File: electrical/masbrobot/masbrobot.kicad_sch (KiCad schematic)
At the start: 24 parts

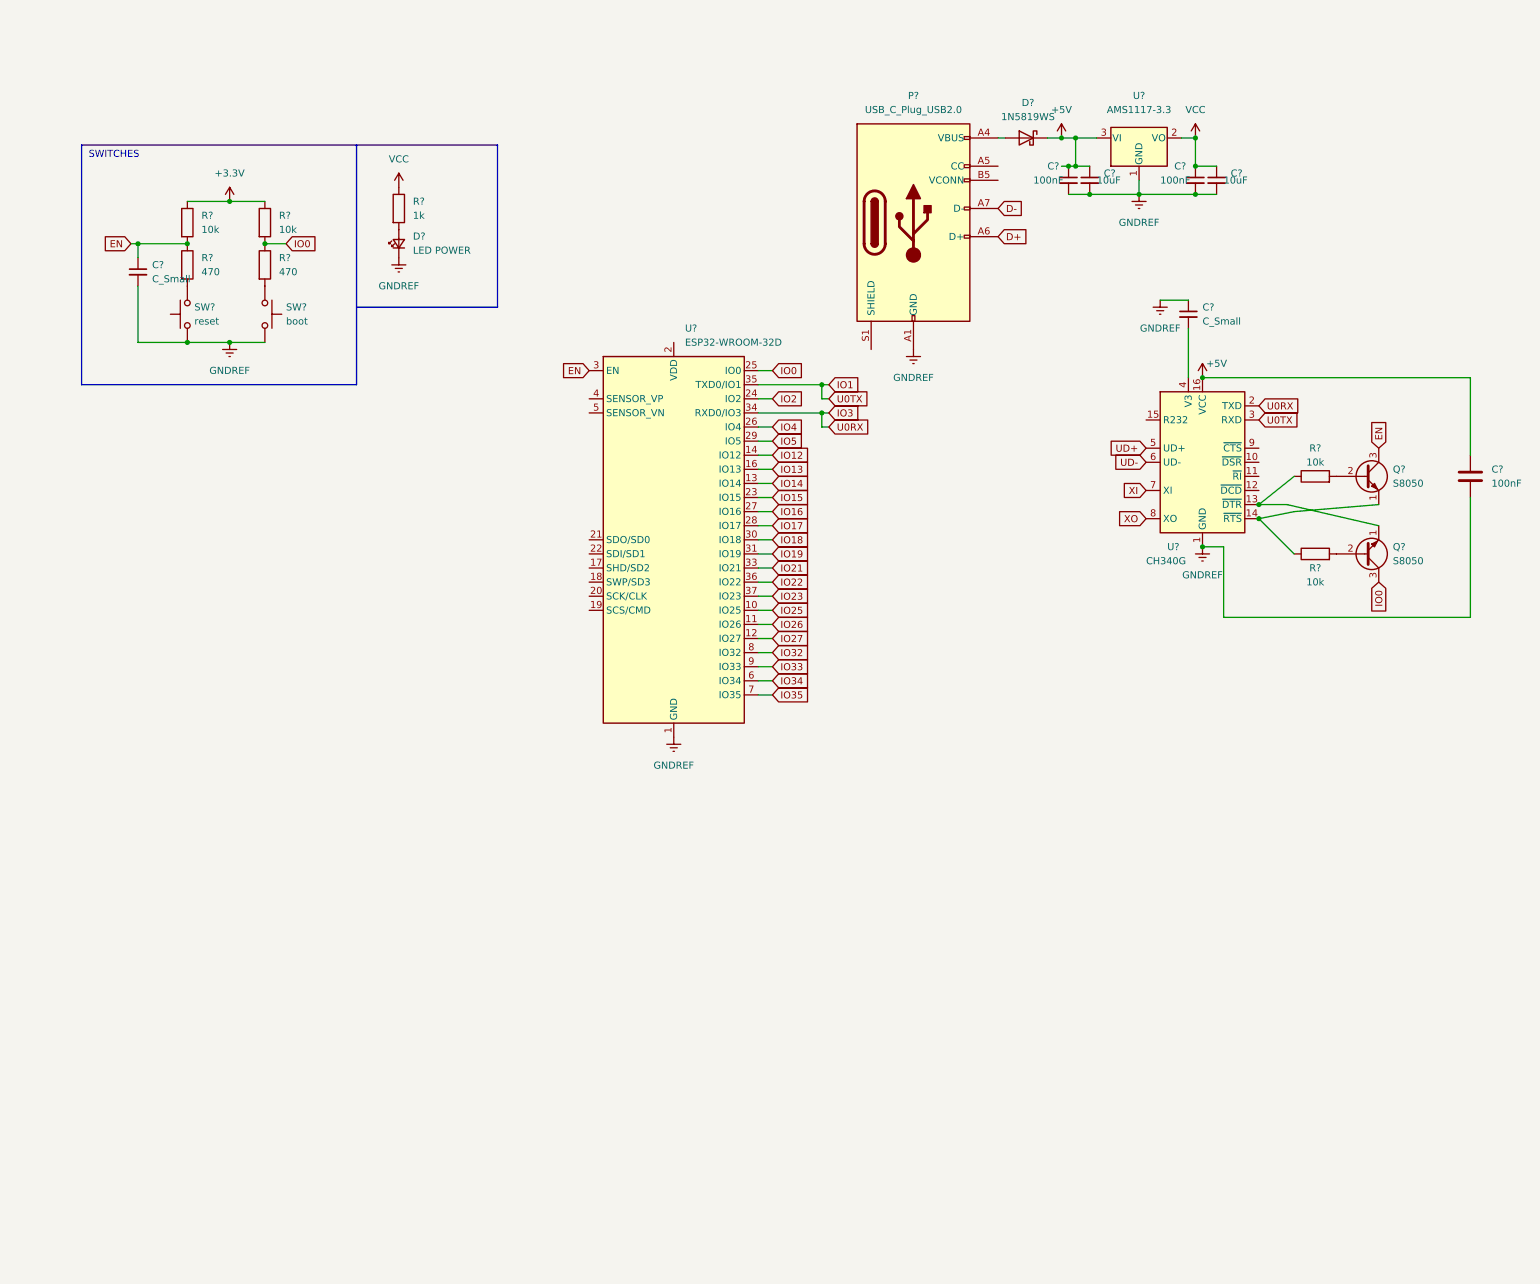
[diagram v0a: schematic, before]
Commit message: adding Gyro schematics, some components, product page link, etc
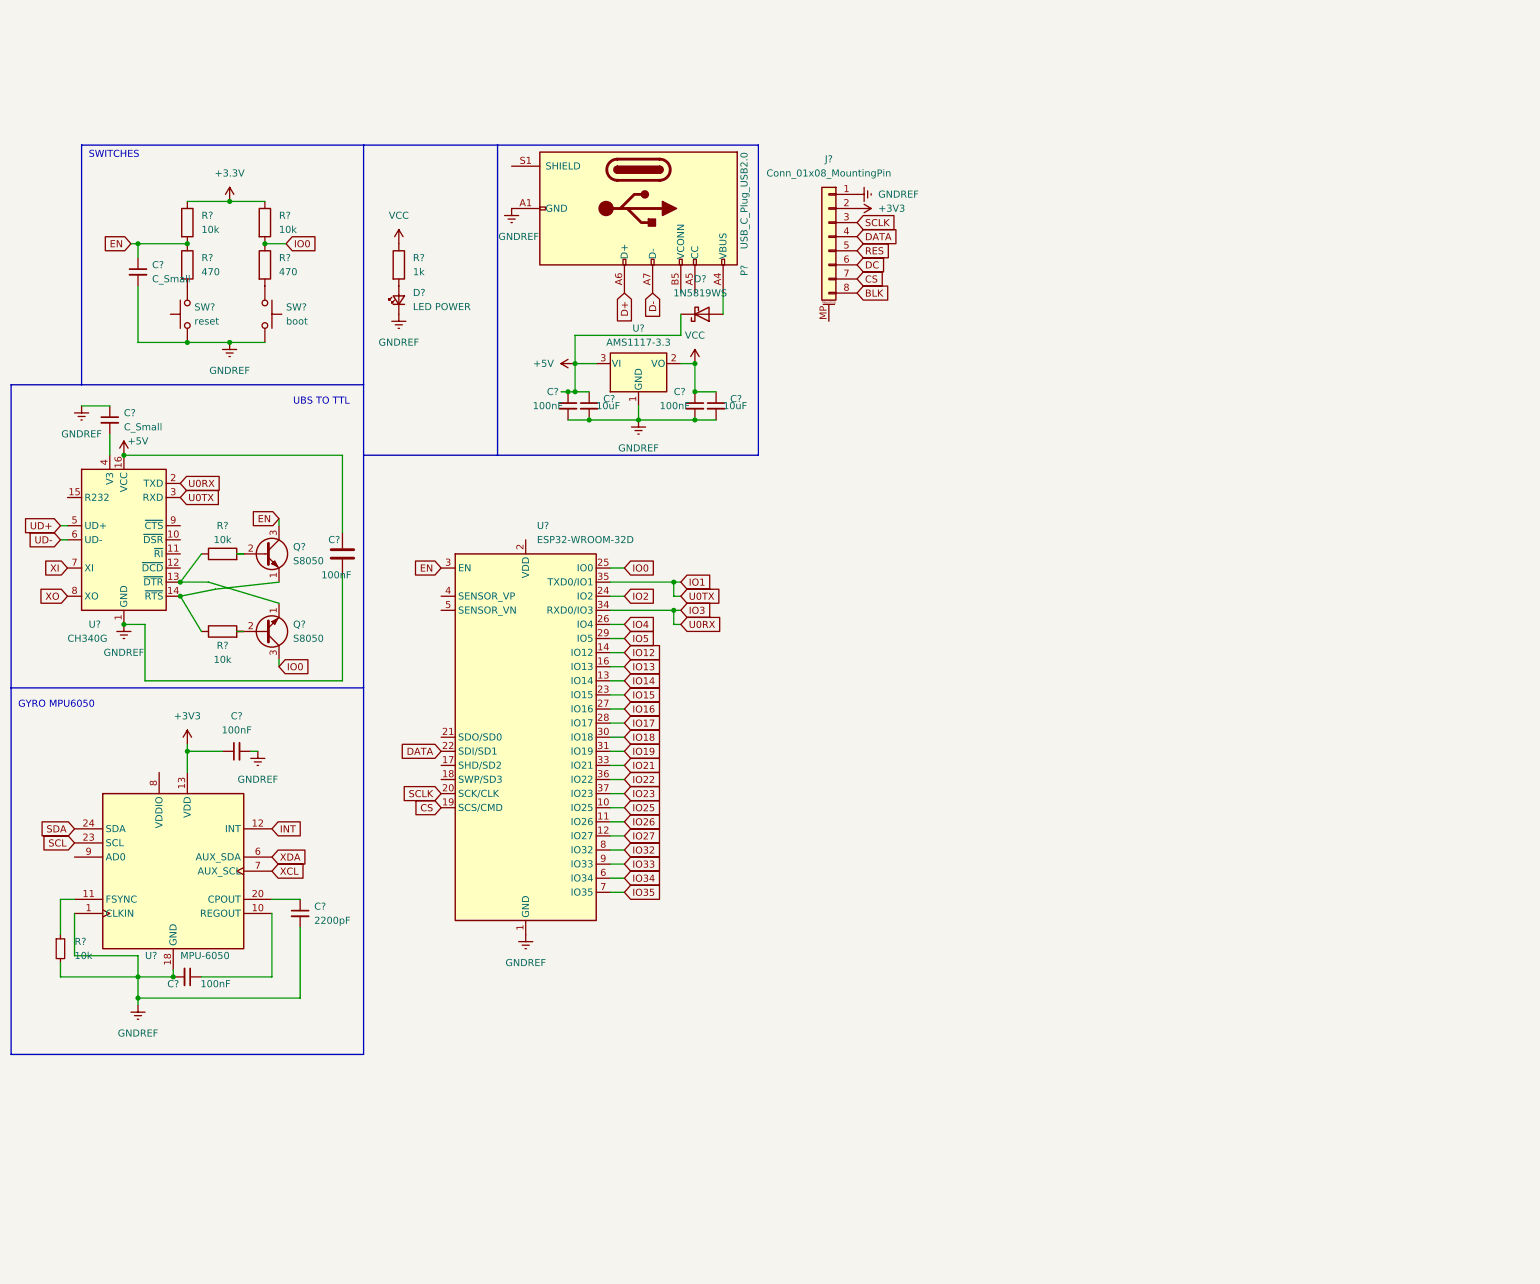
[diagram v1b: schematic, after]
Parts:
- added C? (x2): 100nF, symbol Device:C_Small
- added C?: 2200pF, symbol Device:C_Small
- added J?: Conn_01x08_MountingPin, symbol Connector_Generic_MountingPin:Conn_01x08_MountingPin
- added R?: 10k, symbol Device:R_Small
- added U?: MPU-6050, Sensor_Motion:InvenSense_QFN-24_4x4mm_P0.5mm, symbol Sensor_Motion:MPU-6050
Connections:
- net GNDREF: now also C?.2, C?.2, C?.2, J?.1 (Pin_1), R?.2, U?.1 (CLKIN), U?.18 (GND)
- net CS: now reaches U?.19 (SCS/CMD)
- net CS: now also J?.7 (Pin_7)
- net SCLK: now reaches U?.20 (SCK/CLK)
- net SCLK: now also J?.3 (Pin_3)
- net DATA: now reaches U?.22 (SDI/SD1)
- net DATA: now also J?.4 (Pin_4)
- new net: C?.1, U?.10 (REGOUT)
- new net: C?.1, U?.20 (CPOUT)
- new net: R?.1, U?.11 (FSYNC)
- new net +3V3: C?.1, J?.2 (Pin_2), U?.13 (VDD)
- new net BLK: J?.8 (Pin_8)
- new net DC: J?.6 (Pin_6)
- new net INT: U?.12 (INT)
- new net RES: J?.5 (Pin_5)
- new net SCL: U?.23 (SCL)
- new net SDA: U?.24 (SDA)
- new net XCL: U?.7 (AUX_SCL)
- new net XDA: U?.6 (AUX_SDA)
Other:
- note added: "GYRO MPU6050"
- note added: "UBS TO TTL"
- moved on the sheet: C?, D?, P?, Q?, R?, U?

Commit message: update schematic and PCB board
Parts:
- removed P?: USB_C_Plug_USB2.0, symbol Connector:USB_C_Plug_USB2.0
- added J1: TYPE-C-31-M-12, HRO_TYPE-C-31-M-12, symbol TYPE-C-31-M-12:TYPE-C-31-M-12
- C1, C2: renamed from C?; value C_Small -> 100nF
- C10, C8: renamed from C?; footprint (none) -> Capacitor_SMD:C_0201_0603Metric
- C7, C9: renamed from C?; footprint (none) -> Capacitor_SMD:C_0805_2012Metric
- D1: renamed from D?; footprint (none) -> LED_SMD:LED_0201_0603Metric
- J2: renamed from J?; footprint (none) -> Connector_PinHeader_1.00mm:PinHeader_1x08_P1.00mm_Horizontal
- R1, R3, R6, R7: renamed from R?; footprint (none) -> Resistor_SMD:R_1206_3216Metric
- R8: renamed from R?; footprint (none) -> Resistor_SMD:R_0201_0603Metric
- SW1, SW2: renamed from SW?; footprint (none) -> Button_Switch_SMD:SW_Tactile_SPST_NO_Straight_CK_PTS636Sx25SMTRLFS
- gave numbers to parts that had none: 14
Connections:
- net IO21 is gone; now on net SDA: U3.33 (IO21)
- net IO22 is gone; now on net SCL: U3.36 (IO22)
- net UD+ is gone; now on net D+: U1.5 (UD+)
- net UD- is gone; now on net D-: U1.6 (UD-)
- net +3.3V: now also U3.2 (VDD)
- net D+: now also J1.A6 (DP1)
- net D-: now also J1.A7 (DN1)
- net GNDREF: now also J1.A1_B12 (GND), J1.B1_A12 (GND)
- net at D2.2 (A): now also J1.A4_B9 (VBUS), J1.B4_A9 (VBUS)
- new net: J1.S1 (SHIELD), J1.S2 (SHIELD), J1.S3 (SHIELD), J1.S4 (SHIELD)
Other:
- moved on the sheet: U3

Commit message: update electrial FIX.
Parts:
- added C11, C12, C7: 100nF, Capacitor_SMD:C_0805_2012Metric, symbol Device:C_Small
- added C14, C9: 10uF, Capacitor_SMD:C_0201_0603Metric, symbol Device:C_Small
- added D10, D3, D4, D5, D6, D7, D8, D9: 1N4007, Diode_SMD:D_0201_0603Metric, symbol Diode:1N4007
- added J2: connector battery 2S Li-Po, Connector_JST:JST_XH_S3B-XH-A-1_1x03_P2.50mm_Horizontal, symbol Connector:Conn_01x03_Socket
- added J3: Micro_SD_Card, Connector_Card:microSD_HC_Hirose_DM3BT-DSF-PEJS, symbol Connector:Micro_SD_Card
- added J5, J6: Conn_01x06, Connector_JST:JST_GH_BM06B-GHS-TBT_1x06-1MP_P1.25mm_Vertical, symbol Connector_Generic:Conn_01x06
- added J7: OLED_128x64_I2C, Connector_JST:JST_GH_BM04B-GHS-TBT_1x04-1MP_P1.25mm_Vertical, symbol Connector:Conn_01x04_Socket
- added U4: L298P, L298P:SOIC127P1420X360-20N, symbol Driver_Motor:L298P
- added U5: AMS1117-5.0, Package_TO_SOT_SMD:SOT-223-3_TabPin2, symbol Regulator_Linear:AMS1117-5.0
- C1, C2, C3, C4, C5, C6: footprint (none) -> Capacitor_SMD:C_0805_2012Metric
- D2: renamed from D1; footprint LED_SMD:LED_0201_0603Metric -> LED_SMD:LED_1206_3216Metric
- J1: footprint HRO_TYPE-C-31-M-12 -> TYPE-C-31-M-12:HRO_TYPE-C-31-M-12
- J4: renamed from J2; value Conn_01x08_MountingPin -> IO; footprint Connector_PinHeader_1.00mm:PinHeader_1x08_P1.00mm_Horizontal -> Connector_PinHeader_1.27mm:PinHeader_1x08_P1.27mm_Horizontal
- R1: renamed from R2; footprint (none) -> Resistor_SMD:R_0805_2012Metric
- R4, R5: footprint (none) -> Resistor_SMD:R_0805_2012Metric
- R8: value 1k -> R_LED; footprint Resistor_SMD:R_0201_0603Metric -> Resistor_SMD:R_0402_1005Metric
- renumbered C8 to C10, C9 to C13, C10 to C15, C7 to C8, D2 to D1, R1 to R2, U4 to U6
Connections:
- net +3V3 is gone; now on net +3.3V: C4.1, J4.2 (Pin_2), U2.13 (VDD)
- net BLK is gone; now on net IO35: J4.8 (Pin_8)
- net DC is gone; now on net IO33: J4.6 (Pin_6)
- net IO5 is gone; now on net CS: U3.29 (IO5)
- net RES is gone; now on net IO33: J4.5 (Pin_5)
- net VCC is gone; now on net +3.3V: C13.1, C15.1, R8.1, U6.2 (VO)
- net +3.3V: now also J5.2 (Pin_2), J6.2 (Pin_2)
- net +5V: now also C11.2, C12.1, C14.1, D3.1 (K), D4.1 (K), D5.1 (K), D6.1 (K), J3.4 (VDD), J7.1 (Pin_1), U4.14 (EnB), U4.6 (Vs), U4.8 (EnA), U5.2 (VO)
- net CS: now also J3.2 (DAT3/CD); no longer J4.7 (Pin_7)
- net DATA: no longer J4.4 (Pin_4)
- net GNDREF: now also C11.1, C12.2, C14.2, C7.2, C9.2, D10.2 (A), D7.2 (A), D8.2 (A), D9.2 (A), J2.1 (Pin_1), J3.6 (VSS), J5.5 (Pin_5), J6.5 (Pin_5), J7.4 (Pin_4), U4.1 (GND), U4.10 (GND), U4.11 (GND), U4.19 (SENSE_B), U4.2 (SENSE_A), U4.20 (GND), U5.1 (GND)
- net IO0: no longer U3.25 (IO0)
- net IO27: now also J4.3 (Pin_3)
- net IO32: now also J4.4 (Pin_4)
- net IO34: now also J4.7 (Pin_7)
- net SCL: now also J7.3 (Pin_3)
- net SCLK: no longer J4.3 (Pin_3)
- net SDA: now also J7.2 (Pin_2)
- net IO12 renamed IN4
- net IN4: now also U4.15 (IN4)
- net IO18 renamed SCK
- net SCK: now also J3.5 (CLK)
- net IO19 renamed MISO
- net MISO: now also J3.7 (DAT0)
- net IO2 renamed IN2
- net IN2: now also U4.9 (IN2)
- net IO23 renamed MOSI
- net MOSI: now also J3.3 (CMD)
- net IO4 renamed IN3
- net IN3: now also U4.13 (IN3)
- net XI: no longer names the net of U1.7 (XI)
- net XO: no longer names the net of U1.8 (XO)
- new net +7.5V: C7.1, C9.1, J2.3 (Pin_3), U4.12 (Vss), U5.3 (VI)
- new net EN1A: J6.3 (Pin_3)
- new net EN1B: J6.4 (Pin_4)
- new net EN2A: J5.3 (Pin_3)
- new net EN2B: J5.4 (Pin_4)
- new net IN1: U3.25 (IO0), U4.7 (IN1)
- new net M1A: D3.2 (A), D7.1 (K), J6.1 (Pin_1), U4.4 (OUT1)
- new net M1B: D4.2 (A), D8.1 (K), J6.6 (Pin_6), U4.5 (OUT2)
- new net M2A: D5.2 (A), D9.1 (K), J5.1 (Pin_1), U4.16 (OUT3)
- new net M2B: D10.1 (K), D6.2 (A), J5.6 (Pin_6), U4.17 (OUT4)
- no-connect marks 0 -> 26
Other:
- note added: "Connectors"
- note added: "LED INDICATOR"
- note added: "Micro SD"
- note added: "Microcontroller"
- note added: "Motor Driver L298P"
- note added: "POWER"
- note added: "reserved ext I/O"
- company: (none) -> TRKB/FTMM/Universitas Airlangga
- title: (none) -> Schematic Masbrobot, PCB 1
- moved on the sheet: C1, C10, C13, C15, C2, C3, C4, C5, C6, C8, D1, D2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

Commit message: update smentara
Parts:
- J2: footprint Connector_JST:JST_XH_S3B-XH-A-1_1x03_P2.50mm_Horizontal -> Connector_JST:JST_XH_B3B-XH-A_1x03_P2.50mm_Vertical
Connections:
- net IO13 is gone; now on net EN1A: U3.16 (IO13)
- net IO14 is gone; now on net EN1B: U3.13 (IO14)
- net IO15 is gone; now on net EN2A: U3.23 (IO15)
- net IO16 is gone; now on net EN2B: U3.27 (IO16)
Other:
- title: Schematic Masbrobot, PCB 1 -> Schematic Masbrobot
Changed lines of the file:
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@@
   (paper "User" 279.4 279.4)
   (title_block
-    (title "Schematic Masbrobot, PCB 1")
+    (title "Schematic Masbrobot")
     (date "2023-05-31")
     (rev "0.1")
@@
   )
   (wire (pts (xy 104.14 87.63) (xy 104.14 101.6))
-    (stroke (width 0) (type default))
+    (stroke (width 0) (type default) (color 255 0 7 1))
   )
   (polyline (pts (xy 182.88 167.64) (xy 182.88 77.47))
@@
   )
   (wire (pts (xy 64.77 87.63) (xy 104.14 87.63))
-    (stroke (width 0) (type default))
+    (stroke (width 0) (type default) (color 255 0 2 1))
   )
   (wire (pts (xy 149.86 138.43) (xy 152.4 138.43))
@@
     (effects (font (size 1.27 1.27)) (justify left bottom))
   )
-  (global_label "IO15" (shape input) (at 152.4 115.57 0) (fields_autoplaced)
-    (effects (font (size 1.27 1.27)) (justify left))
-    (property "Intersheetrefs" "${INTERSHEET_REFS}" (at 159.1674 115.4906 0)
+  (global_label "EN2A" (shape input) (at 152.4 115.57 0) (fields_autoplaced)
+    (effects (font (size 1.27 1.27)) (justify left))
+    (property "Intersheetrefs" "${INTERSHEET_REFS}" (at 160.0834 115.57 0)
       (effects (font (size 1.27 1.27)) (justify left) hide)
     )
@@
     )
   )
-  (global_label "IO13" (shape input) (at 152.4 110.49 0) (fields_autoplaced)
-    (effects (font (size 1.27 1.27)) (justify left))
-    (property "Intersheetrefs" "${INTERSHEET_REFS}" (at 159.1674 110.4106 0)
-      (effects (font (size 1.27 1.27)) (justify left) hide)
-    )
-  )
-  (global_label "IO16" (shape input) (at 152.4 118.11 0) (fields_autoplaced)
-    (effects (font (size 1.27 1.27)) (justify left))
-    (property "Intersheetrefs" "${INTERSHEET_REFS}" (at 159.1674 118.0306 0)
+  (global_label "EN1A" (shape input) (at 152.4 110.49 0) (fields_autoplaced)
+    (effects (font (size 1.27 1.27)) (justify left))
+    (property "Intersheetrefs" "${INTERSHEET_REFS}" (at 160.0834 110.49 0)
+      (effects (font (size 1.27 1.27)) (justify left) hide)
+    )
+  )
+  (global_label "EN2B" (shape input) (at 152.4 118.11 0) (fields_autoplaced)
+    (effects (font (size 1.27 1.27)) (justify left))
+    (property "Intersheetrefs" "${INTERSHEET_REFS}" (at 160.2648 118.11 0)
       (effects (font (size 1.27 1.27)) (justify left) hide)
     )
@@
     )
   )
-  (global_label "IO14" (shape input) (at 152.4 113.03 0) (fields_autoplaced)
-    (effects (font (size 1.27 1.27)) (justify left))
-    (property "Intersheetrefs" "${INTERSHEET_REFS}" (at 159.1674 112.9506 0)
+  (global_label "EN1B" (shape input) (at 152.4 113.03 0) (fields_autoplaced)
+    (effects (font (size 1.27 1.27)) (justify left))
+    (property "Intersheetrefs" "${INTERSHEET_REFS}" (at 160.2648 113.03 0)
       (effects (font (size 1.27 1.27)) (justify left) hide)
     )
@@
       (effects (font (size 1.27 1.27)))
     )
-    (property "Footprint" "Connector_JST:JST_XH_S3B-XH-A-1_1x03_P2.50mm_Horizontal" (at 156.21 66.04 0)
+    (property "Footprint" "Connector_JST:JST_XH_B3B-XH-A_1x03_P2.50mm_Vertical" (at 156.21 66.04 0)
       (effects (font (size 1.27 1.27)) hide)
     )
